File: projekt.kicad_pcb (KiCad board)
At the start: 4 copper layers, 65 x 65 mm, 117 parts, among them IC1 DW01+G, IC4 MIC5504-3.3YM5-TR, J10 Conn_01x06_Pin, J2 TP4056, J4 Conn_01x02_Socket, J6 USB_C_Receptacle_PowerOnly_24P, Q1 AO3400A, Q2 AO3400A, Q3 AO3400A, Q4 AO3400A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

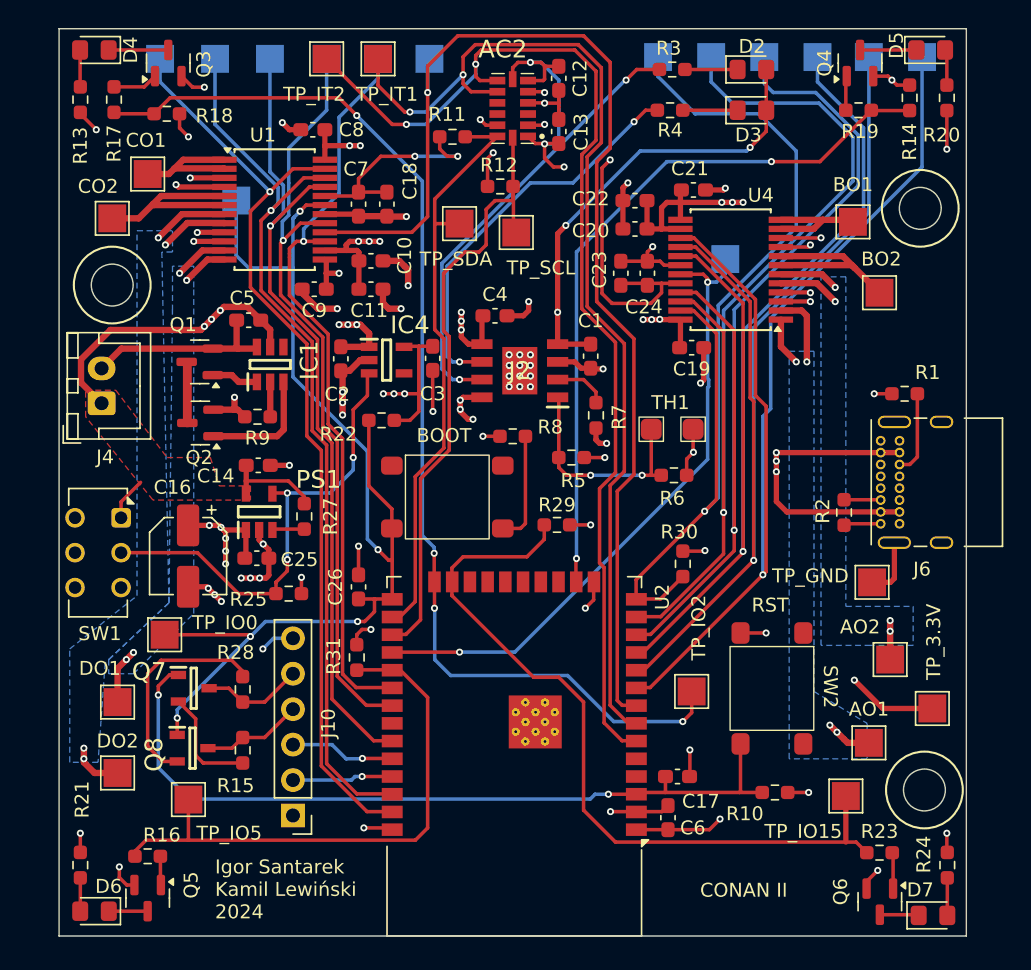
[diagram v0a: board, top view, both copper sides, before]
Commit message: Poprawione dziury montażowe
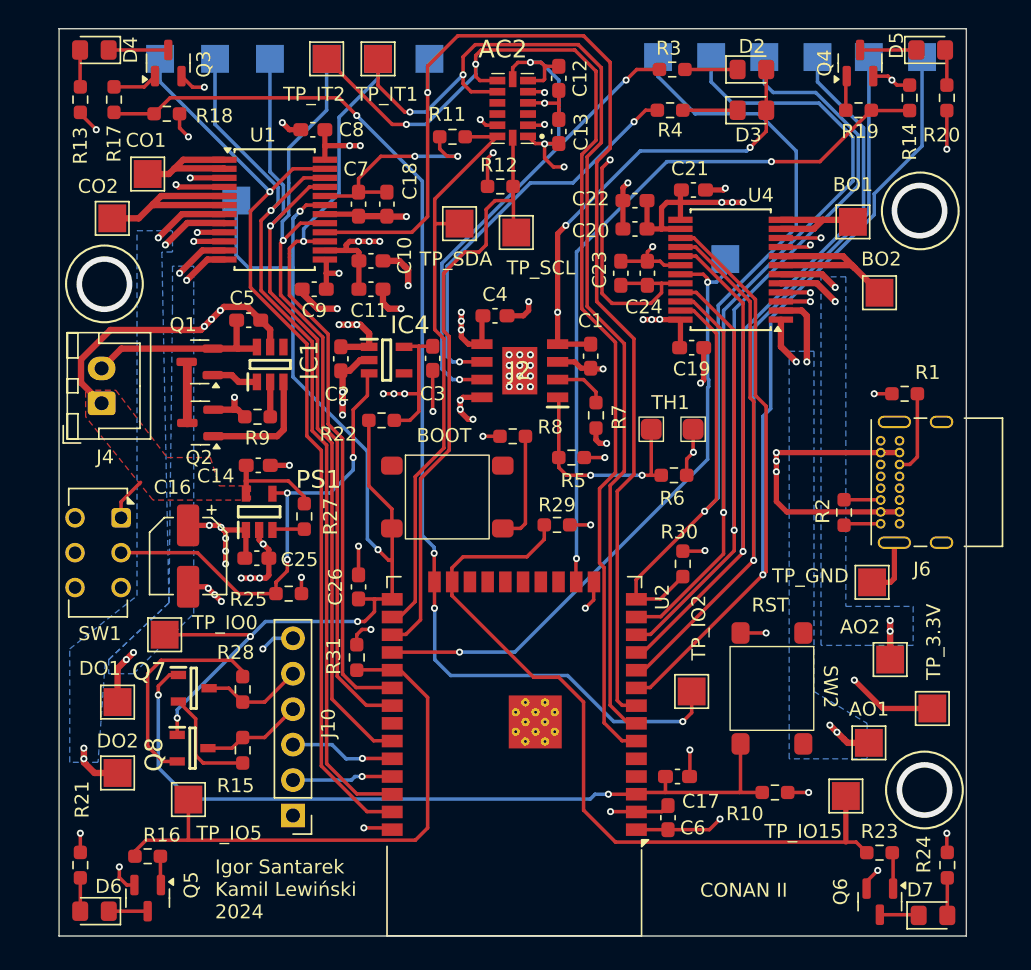
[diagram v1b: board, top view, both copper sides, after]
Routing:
- net GND: vias 66 -> 69
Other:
- outline, holes or cut-outs redrawn
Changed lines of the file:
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@@
 	)
 	(gr_circle
-		(center 180.086 77.387)
-		(end 182.836 77.387)
+		(center 180.086 77.5716)
+		(end 182.836 77.5716)
 		(stroke
 			(width 0.15)
@@
 	)
 	(gr_circle
-		(center 122.174 82.887)
-		(end 124.924 82.887)
+		(center 121.6152 82.804)
+		(end 124.3652 82.804)
 		(stroke
 			(width 0.15)
@@
 		(layer "Edge.Cuts")
 	)
-	(gr_circle
-		(center 180.384 119.0752)
-		(end 181.884 119.0752)
-		(stroke
-			(width 0.1)
-			(type default)
-		)
-		(fill none)
-		(layer "Edge.Cuts")
-	)
-	(gr_circle
-		(center 122.174 82.887)
-		(end 123.674 82.887)
-		(stroke
-			(width 0.1)
-			(type default)
-		)
-		(fill none)
-		(layer "Edge.Cuts")
-	)
-	(gr_circle
-		(center 180.086 77.387)
-		(end 181.586 77.387)
-		(stroke
-			(width 0.1)
-			(type default)
-		)
-		(fill none)
-		(layer "Edge.Cuts")
-	)
 	(gr_text "Igor Santarek\nKamil Lewiński\n2024"
 		(at 129.54 128.397 0)
@@
 	)
 	(via
+		(at 180.0352 77.553)
+		(size 4)
+		(drill 3.2)
+		(layers "F.Cu" "B.Cu")
+		(free yes)
+		(net 1)
+	)
+	(via
 		(at 131.4196 103.886)
 		(size 0.508)
@@
 	)
 	(via
+		(at 180.3908 119.0752)
+		(size 4)
+		(drill 3.2)
+		(layers "F.Cu" "B.Cu")
+		(free yes)
+		(net 1)
+	)
+	(via
 		(at 134.366 71.247)
 		(size 0.508)
@@
 	)
 	(via
+		(at 121.6152 82.8226)
+		(size 4)
+		(drill 3.2)
+		(layers "F.Cu" "B.Cu")
+		(free yes)
+		(net 1)
+	)
+	(via
 		(at 172.974 79.502)
 		(size 0.508)
@@
 	)
 	(segment
+		(start 169.367 85.268)
+		(end 176.784 77.851)
+		(width 0.254)
+		(layer "B.Cu")
+		(net 76)
+	)
+	(segment
+		(start 176.784 76.3524)
+		(end 180.213 72.9234)
+		(width 0.254)
+		(layer "B.Cu")
+		(net 76)
+	)
+	(segment
 		(start 169.367 91.745)
 		(end 169.367 85.268)
@@
 	)
 	(segment
-		(start 169.367 85.268)
-		(end 180.213 74.422)
+		(start 176.784 77.851)
+		(end 176.784 76.3524)
 		(width 0.254)
 		(layer "B.Cu")
@@
 	)
 	(segment
-		(start 168.805 103.654)
-		(end 168.805 92.307)
+		(start 180.213 72.9234)
+		(end 180.213 66.548)
 		(width 0.254)
 		(layer "B.Cu")
@@
 	)
 	(segment
-		(start 180.213 74.422)
-		(end 180.213 66.548)
+		(start 168.805 103.654)
+		(end 168.805 92.307)
 		(width 0.254)
 		(layer "B.Cu")

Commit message: final commit
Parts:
- moved R6 4.76 mm to (158.0, 98.3), turned to -90 degrees
- moved TH1 2.34 mm to (160.4, 94.5), turned to -90 degrees
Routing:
- net /DIN2: track 85.1 -> 88.3 mm
- net /ACC_IT1: track 75.5 -> 78.6 mm
- net /ACC_IT2: track 79.0 -> 82.1 mm
- net Net-(J2-TEMP1): track 15.9 -> 13.2 mm, vias 2 -> 0
- net GND: track 132.2 -> 131.8 mm, vias 69 -> 70

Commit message: final commit2
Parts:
- moved D7 2.21 mm to (178.8, 128.4)
- moved AC2 2.21 mm to (148.7, 70.6)
- moved AO2 2.21 mm to (175.7, 110.1)
- moved BO1 2.21 mm to (173.1, 78.7)
- moved BO2 2.21 mm to (175.0, 83.8)
- moved C1 2.21 mm to (154.3, 88.3)
- moved C21 2.21 mm to (161.6, 76.4)
- moved C22 2.21 mm to (157.5, 77.2)
- moved C8 2.21 mm to (134.4, 72.1)
- moved DO1 2.21 mm to (120.4, 113.1)
- moved DO2 2.21 mm to (120.4, 118.2)
- moved G*** 2.21 mm to (152.4, 102.9)
- moved J6 2.21 mm to (175.1, 100.4)
- moved Q1 2.21 mm to (126.3, 88.8)
- moved R1 2.21 mm to (176.8, 91.0)
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
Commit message: final commit3
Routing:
- added copper zone on B.Cu, net GND
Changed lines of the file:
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@@
 		(polygon
 			(pts
-				(xy 117.1967 65.516332) (xy 180.5697 65.643332) (xy 181.0777 125.206332) (xy 176.5057 125.206332)
+				(xy 116.2823 64.932132) (xy 180.9507 64.982932) (xy 181.3825 125.257132) (xy 176.5057 125.206332)
 				(xy 176.2517 69.834332) (xy 142.5967 69.961332) (xy 142.5967 75.549332) (xy 171.1717 75.295332)
 				(xy 171.2987 93.202332) (xy 155.9317 93.202332) (xy 155.9317 84.185332) (xy 123.1657 84.058332)
 				(xy 123.2292 90.535332) (xy 124.5627 90.535332) (xy 137.2627 90.535332) (xy 137.2627 106.537332)
-				(xy 130.7857 106.537332) (xy 130.7857 123.301332) (xy 124.4357 123.301332) (xy 124.5627 129.651332)
-				(xy 116.9427 129.651332)
+				(xy 130.7857 106.537332) (xy 130.7857 123.301332) (xy 124.4357 123.301332) (xy 124.5627 129.956132)
+				(xy 116.1807 129.905332)
 			)
 		)
@@
 		(polygon
 			(pts
-				(xy 116.9427 65.389332) (xy 180.6967 65.389332) (xy 180.9507 129.524332) (xy 173.5847 129.397332)
-				(xy 173.5847 122.920332) (xy 124.1817 122.920332) (xy 124.1817 129.270332) (xy 116.9427 129.270332)
+				(xy 116.332937 65.211531) (xy 181.001337 65.262331) (xy 181.204537 129.879931) (xy 173.279737 129.829131)
+				(xy 173.279737 123.199731) (xy 124.130737 123.199731) (xy 124.130737 129.905331) (xy 116.2315 129.905332)
 			)
 		)
@@
 		(layer "B.Cu")
 		(hatch edge 0.5)
-		(priority 7)
+		(priority 8)
 		(connect_pads yes
 			(clearance 0.5)
@@
 	)
 	(zone
+		(net 1)
+		(net_name "GND")
+		(layer "B.Cu")
+		(hatch edge 0.5)
+		(connect_pads
+			(clearance 0.25)
+		)
+		(min_thickness 0.25)
+		(filled_areas_thickness no)
+		(fill yes
+			(thermal_gap 0.25)
+			(thermal_bridge_width 0.25)
+		)
+		(polygon
+			(pts
+				(xy 116.3839 64.932132) (xy 181.0523 64.982932) (xy 181.2047 129.854532) (xy 173.2799 129.803732)
+				(xy 173.3307 122.894932) (xy 124.5119 122.996532) (xy 124.5119 129.905332) (xy 116.2315 129.905332)
+			)
+		)
+	)
+	(zone
 		(net 80)
 		(net_name "Net-(AO2-Pin_1)")
 		(layer "B.Cu")
 		(hatch edge 0.5)
-		(priority 1)
+		(priority 8)
 		(connect_pads yes
 			(clearance 0.5)

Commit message: final commit5
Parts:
- removed J6: USB_C_Receptacle_PowerOnly_24P, Connector_USB:USB_C_Receptacle_GCT_USB4085
- removed R1, R2: 5.1k, Resistor_SMD:R_0603_1608Metric_Pad0.98x0.95mm_HandSolder
- added J1: 10118194-0001LF, SamacSys_Parts:101181940001LF, F.Cu at (179.1, 96.7)
- added R26: 10k, Resistor_SMD:R_0603_1608Metric_Pad0.98x0.95mm_HandSolder, F.Cu at (172.7, 98.3)
- added R32: 10k, Resistor_SMD:R_0603_1608Metric_Pad0.98x0.95mm_HandSolder, F.Cu at (172.7, 94.6)
- D2: value LED -> GREEN
- D3: value LED -> RED
- moved D3 1.19 mm to (164.7, 70.6)
- moved D2 1.19 mm to (164.7, 67.8)
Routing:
- net GND: track 131.8 -> 138.7 mm, vias 70 -> 73
- net VCC: track 59.3 -> 52.6 mm, vias 10 -> 9
- net Net-(J6-CC2): track 6.03 -> 0.00 mm
- net Net-(J1-D+): track 0.00 -> 4.50 mm
- net Net-(J1-D-): track 0.00 -> 4.02 mm
- net Net-(J6-CC1): track 2.63 -> 0.00 mm
- net Net-(D2-K): track 3.78 -> 2.60 mm
- net Net-(D3-K): track 3.93 -> 2.79 mm
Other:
- board text added: "CHRG"
- board text added: "STBY"

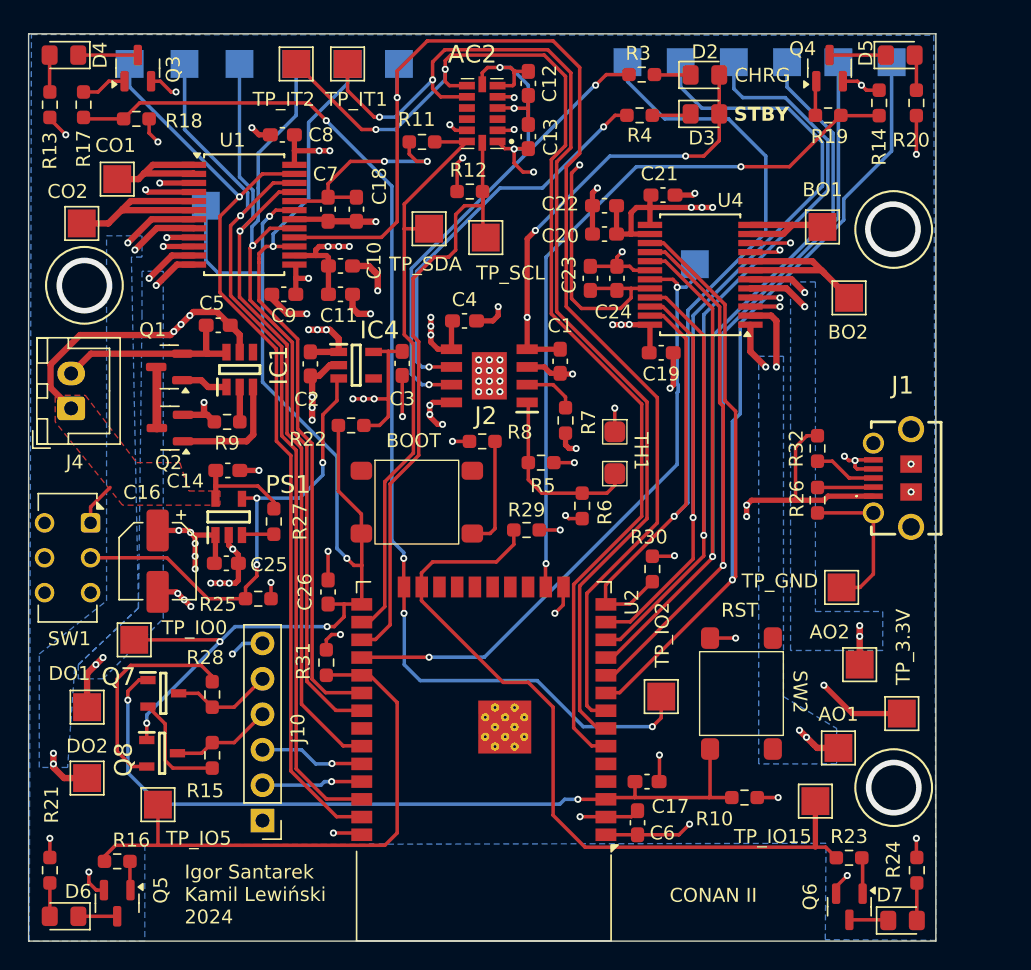
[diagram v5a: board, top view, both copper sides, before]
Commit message: Podmiana tranzystorów
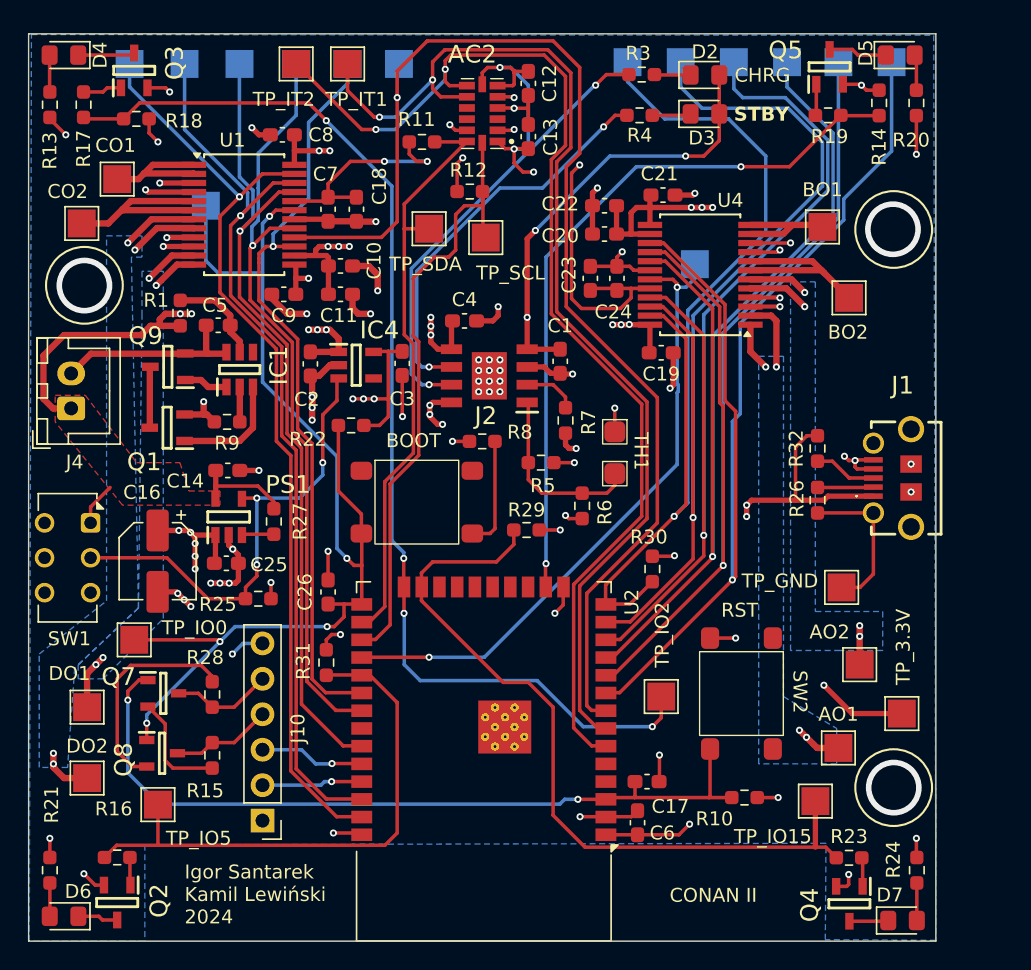
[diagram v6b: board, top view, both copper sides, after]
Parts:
- removed Q6: AO3400A, Package_TO_SOT_SMD:SOT-23
- added Q9: AO3420, SamacSys_Parts:SOT95P280X125-3N, F.Cu at (126.2, 88.7)
- added R1: 470, Resistor_SMD:R_0603_1608Metric_Pad0.98x0.95mm_HandSolder, F.Cu at (127.1, 84.9)
- Q1, Q2, Q3, Q4, Q5: value AO3400A -> AO3420; footprint Package_TO_SOT_SMD:SOT-23 -> SamacSys_Parts:SOT95P280X125-3N
- moved Q5 78.7 mm to (173.6, 67.2), turned to 90 degrees
- moved Q4 59.9 mm to (175.0, 127.2), turned to -90 degrees
- moved Q2 34.2 mm to (122.5, 127.1), turned to -90 degrees
- moved Q1 4.36 mm to (126.1, 93.1)
- moved Q3 0.30 mm to (123.7, 67.5)
- moved R16 0.28 mm to (122.5, 123.9)
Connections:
- C5 pad 2: /LIPO+ -> Net-(IC1-VCC)
- IC1 pad 5: /LIPO+ -> Net-(IC1-VCC)
- Q1 pad 1: Net-(IC1-OD) -> Net-(IC1-OC)
- Q1 pad 2: /LIPO- -> GND
- Q2 pad 1: Net-(IC1-OC) -> Net-(Q2-G)
- Q2 pad 3: Net-(Q1-D) -> Net-(D6-K)
- Q4 pad 3: Net-(D5-K) -> Net-(D7-K)
- Q5 pad 3: Net-(D6-K) -> Net-(D5-K)
- R16 pad 1: Net-(Q5-G) -> Net-(Q2-G)
- R19 pad 1: Net-(Q4-G) -> Net-(Q5-G)
- R23 pad 1: Net-(Q6-G) -> Net-(Q4-G)
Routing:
- net Net-(IC1-VCC): track 0.00 -> 6.93 mm
- net Net-(Q6-G): track 2.60 -> 0.00 mm
- net Net-(Q2-G): track 0.00 -> 2.05 mm
- net /LIPO+: track 42.0 -> 40.2 mm, vias 9 -> 8
- net GND: track 138.7 -> 137.9 mm

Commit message: Podmiana tranzystorów i symboli
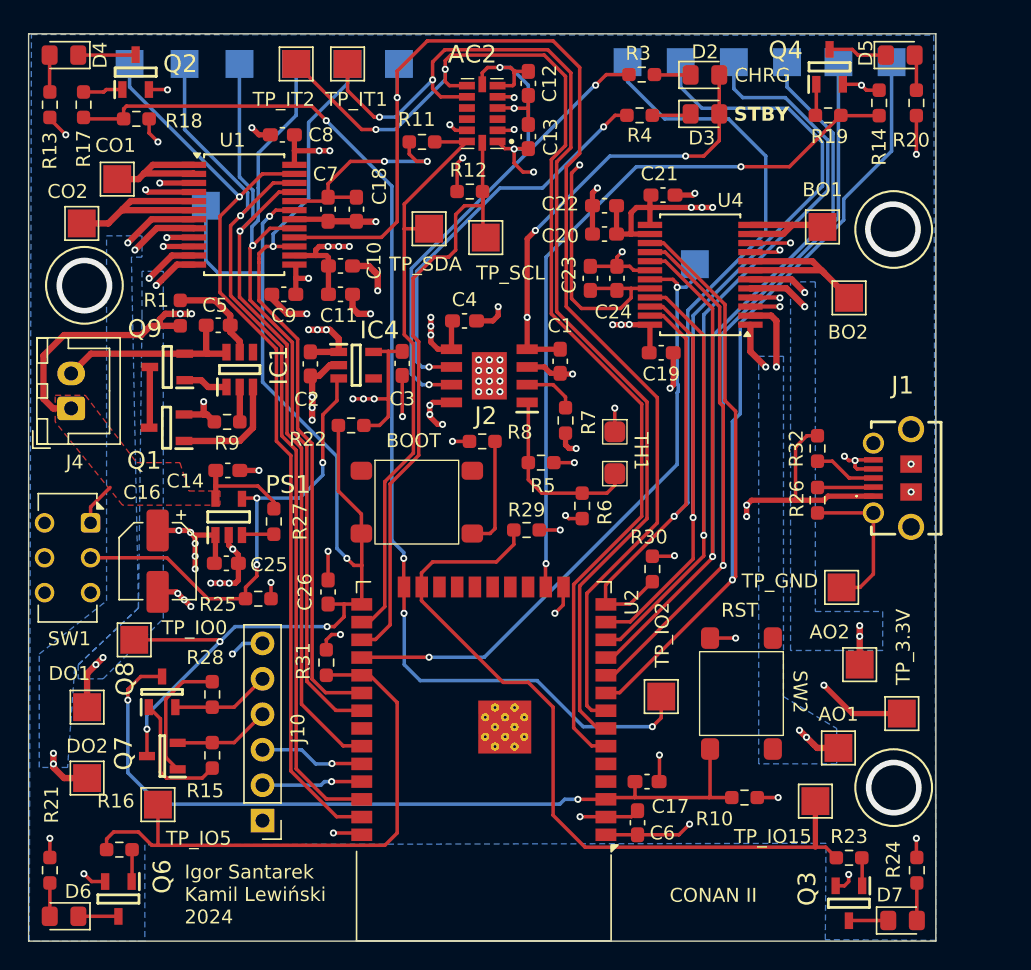
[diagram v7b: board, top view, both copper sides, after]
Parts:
- removed Q5: AO3420, SamacSys_Parts:SOT95P280X125-3N
- added Q6: AO3420, SamacSys_Parts:SOT95P280X125-3N, F.Cu at (122.6, 126.9)
- Q7, Q8: value SS8050-HF -> MMSS8050-H-TP; footprint SamacSys_Parts:SOT95P240X115-3N -> SamacSys_Parts:SOT95P237X125-3N
- moved Q3 78.7 mm to (175.0, 127.2), turned to -90 degrees
- moved Q4 60.0 mm to (173.6, 67.2), turned to 90 degrees
- moved Q2 59.5 mm to (123.9, 67.6), turned to 90 degrees
- moved Q7 4.50 mm to (125.8, 116.6), turned to 180 degrees
- moved Q8 4.40 mm to (125.7, 112.0), turned to 90 degrees
- moved R16 0.58 mm to (122.7, 123.4)
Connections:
- Q2 pad 3: Net-(D6-K) -> Net-(D4-K)
- Q3 pad 3: Net-(D4-K) -> Net-(D7-K)
- Q4 pad 3: Net-(D7-K) -> Net-(D5-K)
- Q7 pad 1: /EN -> Net-(Q7-B)
- Q7 pad 2: Net-(Q7-B) -> /DTR
- Q7 pad 3: /RTS -> /BOOT
- Q8 pad 1: /BOOT -> Net-(Q8-B)
- Q8 pad 2: Net-(Q8-B) -> /RTS
- Q8 pad 3: /DTR -> /EN
- R15 pad 1: Net-(Q7-B) -> Net-(Q8-B)
- R16 pad 1: Net-(Q2-G) -> Net-(Q6-G)
- R17 pad 1: Net-(Q3-G) -> Net-(Q2-G)
- R19 pad 1: Net-(Q5-G) -> Net-(Q4-G)
- R23 pad 1: Net-(Q4-G) -> Net-(Q3-G)
- R28 pad 1: Net-(Q8-B) -> Net-(Q7-B)
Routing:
- net Net-(Q8-B): track 15.7 -> 9.18 mm
- net Net-(Q6-G): track 0.00 -> 2.33 mm
- net Net-(Q5-G): track 2.25 -> 0.00 mm
- net Net-(Q7-B): track 7.97 -> 9.24 mm
- net /EN: track 56.8 -> 58.0 mm
- net /BOOT: track 80.7 -> 81.9 mm
- net /LED2: track 39.9 -> 40.7 mm
- net Net-(Q2-G): track 2.05 -> 2.86 mm
- net Net-(Q3-G): track 2.80 -> 2.11 mm
